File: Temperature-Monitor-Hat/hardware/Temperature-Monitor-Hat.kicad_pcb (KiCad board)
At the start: 2 copper layers, 80.3 x 36.1 mm, 8 parts, among them J1 TEENSY3.2-72MHz, J2 THERMO, U1 MAX31855

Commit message: Ordered boards, parts, and stencil.
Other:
- board text added: "Temperature Monitor Teensy Hat v1.0 7/30/2016"
- board text removed: "Temperature Monitor Teensy Hat 7/30/2016"
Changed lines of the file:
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@@
     (visible_elements FFFEDF7D)
     (pcbplotparams
-      (layerselection 0x20010_00000000)
+      (layerselection 0x210fc_80000001)
       (usegerberextensions true)
       (excludeedgelayer true)
@@
     (effects (font (size 1.5 1.5) (thickness 0.3)) (justify mirror))
   )
-  (gr_text "Temperature Monitor Teensy Hat \n7/30/2016" (at 149.3012 99.9236) (layer B.SilkS)
+  (gr_text "Temperature Monitor Teensy Hat  v1.0\n7/30/2016" (at 149.3012 99.9236) (layer B.SilkS)
     (effects (font (size 1.5 1.5) (thickness 0.3)) (justify mirror))
   )

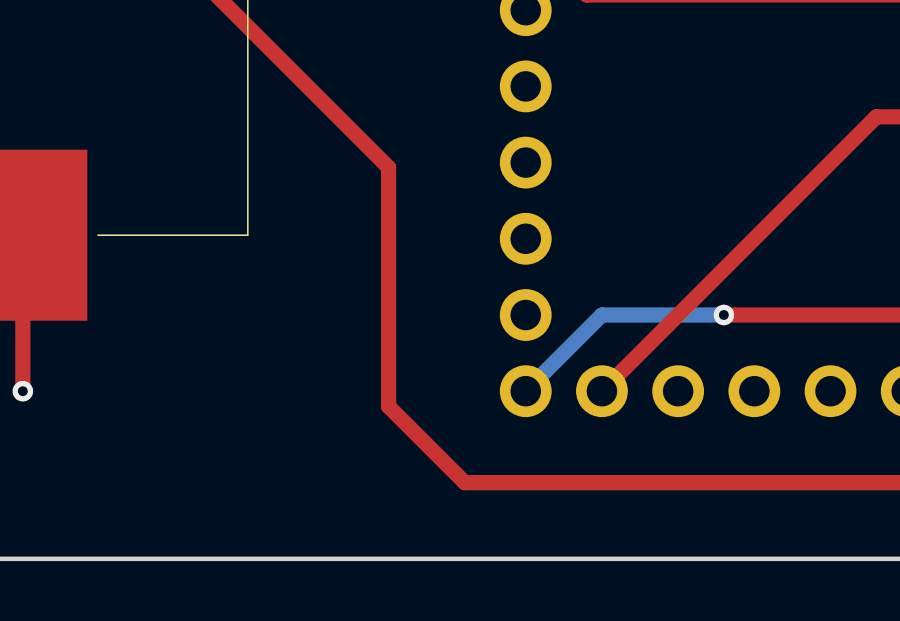
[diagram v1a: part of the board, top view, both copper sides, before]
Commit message: Added board outline to assembly diagrams.
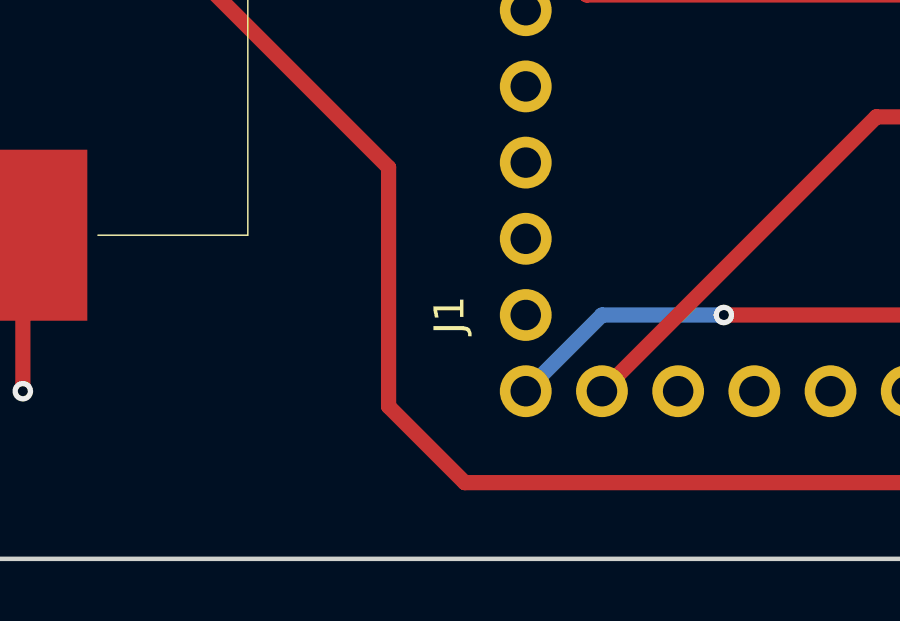
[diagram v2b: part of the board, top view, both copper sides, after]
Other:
- board text added: "7/30/2016"
- board text added: "Temperature Monitor Teensy Hat v1.0"
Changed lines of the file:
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@@
     (links 29)
     (no_connects 1)
-    (area 97.852159 74.854999 178.510001 123.265001)
+    (area 97.852159 72.922 178.510001 123.265001)
     (thickness 1.6)
-    (drawings 28)
+    (drawings 34)
     (tracks 102)
     (zones 0)
@@
     (visible_elements FFFEDF7D)
     (pcbplotparams
-      (layerselection 0x210fc_80000001)
+      (layerselection 0x30000_00000000)
       (usegerberextensions true)
       (excludeedgelayer true)
@@
     (fp_line (start 6.5 -11.5) (end -11.5 -11.5) (layer F.Fab) (width 0.05))
     (fp_line (start 6.5 24) (end 6.5 -11.5) (layer F.Fab) (width 0.05))
-    (fp_text user %R (at 2.54 25.4 270) (layer F.SilkS) hide
+    (fp_text user %R (at 2.54 25.4 270) (layer F.SilkS)
       (effects (font (size 1 1) (thickness 0.15)))
     )
@@
     (pad 15 thru_hole circle (at 5.08 17.78 270) (size 1.7272 1.7272) (drill 1.016) (layers *.Cu *.Mask F.SilkS))
   )
+  (gr_text 7/30/2016 (at 170.942 115.824) (layer F.Fab)
+    (effects (font (size 1.5 1.5) (thickness 0.3)) (justify mirror))
+  )
+  (gr_text "Temperature Monitor Teensy Hat  v1.0" (at 155.702 74.422) (layer F.Fab)
+    (effects (font (size 1.5 1.5) (thickness 0.3)) (justify mirror))
+  )
+  (gr_line (start 178.308 113.538) (end 178.308 77.216) (layer F.Fab) (width 0.2))
+  (gr_line (start 98.044 113.538) (end 178.308 113.538) (layer F.Fab) (width 0.2))
+  (gr_line (start 98.044 77.216) (end 98.044 113.538) (layer F.Fab) (width 0.2))
+  (gr_line (start 178.308 77.216) (end 98.044 77.216) (layer F.Fab) (width 0.2))
   (gr_text wickerbox.net (at 100.5078 94.615 90) (layer B.SilkS)
     (effects (font (size 1.5 1.5) (thickness 0.3)) (justify mirror))
